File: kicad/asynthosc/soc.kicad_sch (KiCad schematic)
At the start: 1 part, among them U2 STM32H723ZGTx

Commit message: sch: wip
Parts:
- added C18, C19, C20, C21, C22, C23, C24, C25, C26, C27, C28: 100n, 0402, symbol Device:C
- added C29: 1u, 0402, symbol Device:C
- added FB2: BLM15PX330SN1D, 0402, symbol Device:FerriteBead
- added J13: RJ45_LED, symbol Connector:RJ45_LED
- added JP1: SolderJumper_2_Bridged, symbol Jumper:SolderJumper_2_Bridged
- added TR1: PT61017PEL, Transformer_SMD:Transformer_Ethernet_Bourns_PT61017PEL, symbol Transformer:PT61017PEL
- added U10: USBLC6-2P6, Package_TO_SOT_SMD:SOT-666, symbol Power_Protection:USBLC6-2P6
- added U9: LAN8742A, Package_DFN_QFN:VQFN-24-1EP_4x4mm_P0.5mm_EP2.5x2.5mm_ThermalVias, symbol Interface_Ethernet:LAN8742A
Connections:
- net 3V3: now also U2.108 (VDD), U2.121 (VDD), U2.131 (VDD), U2.144 (VDD), U2.17 (VDD), U2.30 (VDD), U2.39 (VDD), U2.52 (VDD), U2.62 (VDD), U2.72 (VDD), U2.84 (VDD), C18.1, C19.1, C20.1, C21.1, C22.1, C23.1, C24.1, C25.1, C26.1, C27.1, C28.1, FB2.1, JP1.2 (B)
- net GND: now also U2.107 (VSS), U2.120 (VSS), U2.130 (VSS), U2.16 (VSS), U2.31 (VSSA), U2.38 (VSS), U2.51 (VSS), U2.61 (VSS), U2.83 (VSS), U2.94 (VSS), C18.2, C19.2, C20.2, C21.2, C22.2, C23.2, C24.2, C25.2, C26.2, C27.2, C28.2, C29.2
- net at U2.33 (VDDA): now also FB2.2
- net at U2.6 (VBAT): now also C29.1, JP1.1 (A)
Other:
- moved on the sheet: U2

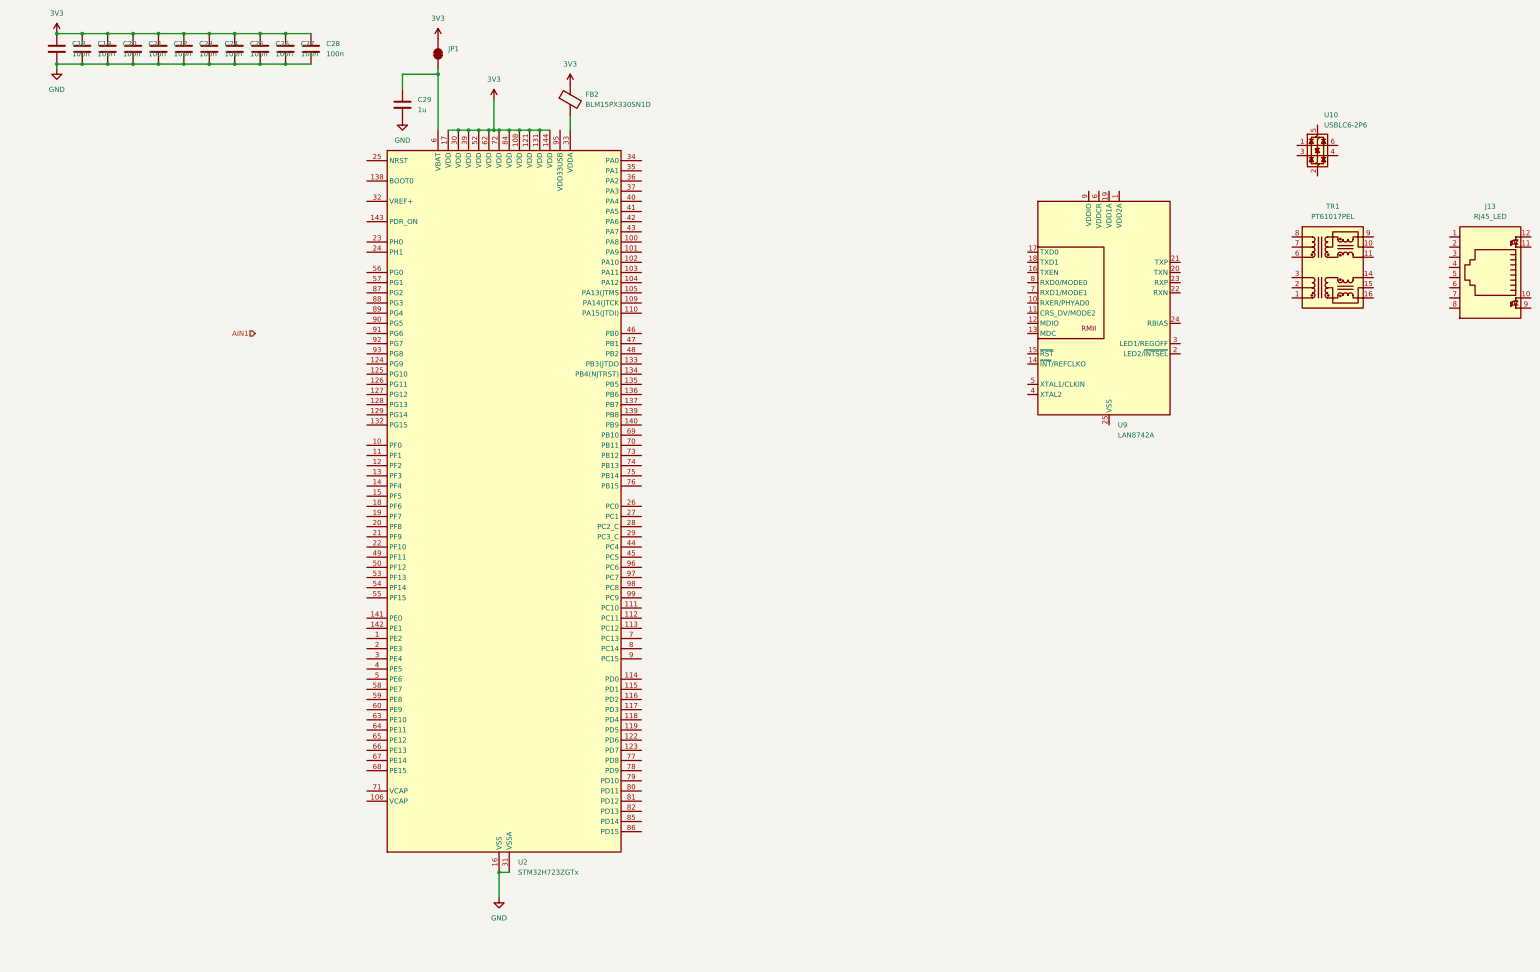
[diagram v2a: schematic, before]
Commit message: sch: basic stm32 with power, clocks and debug
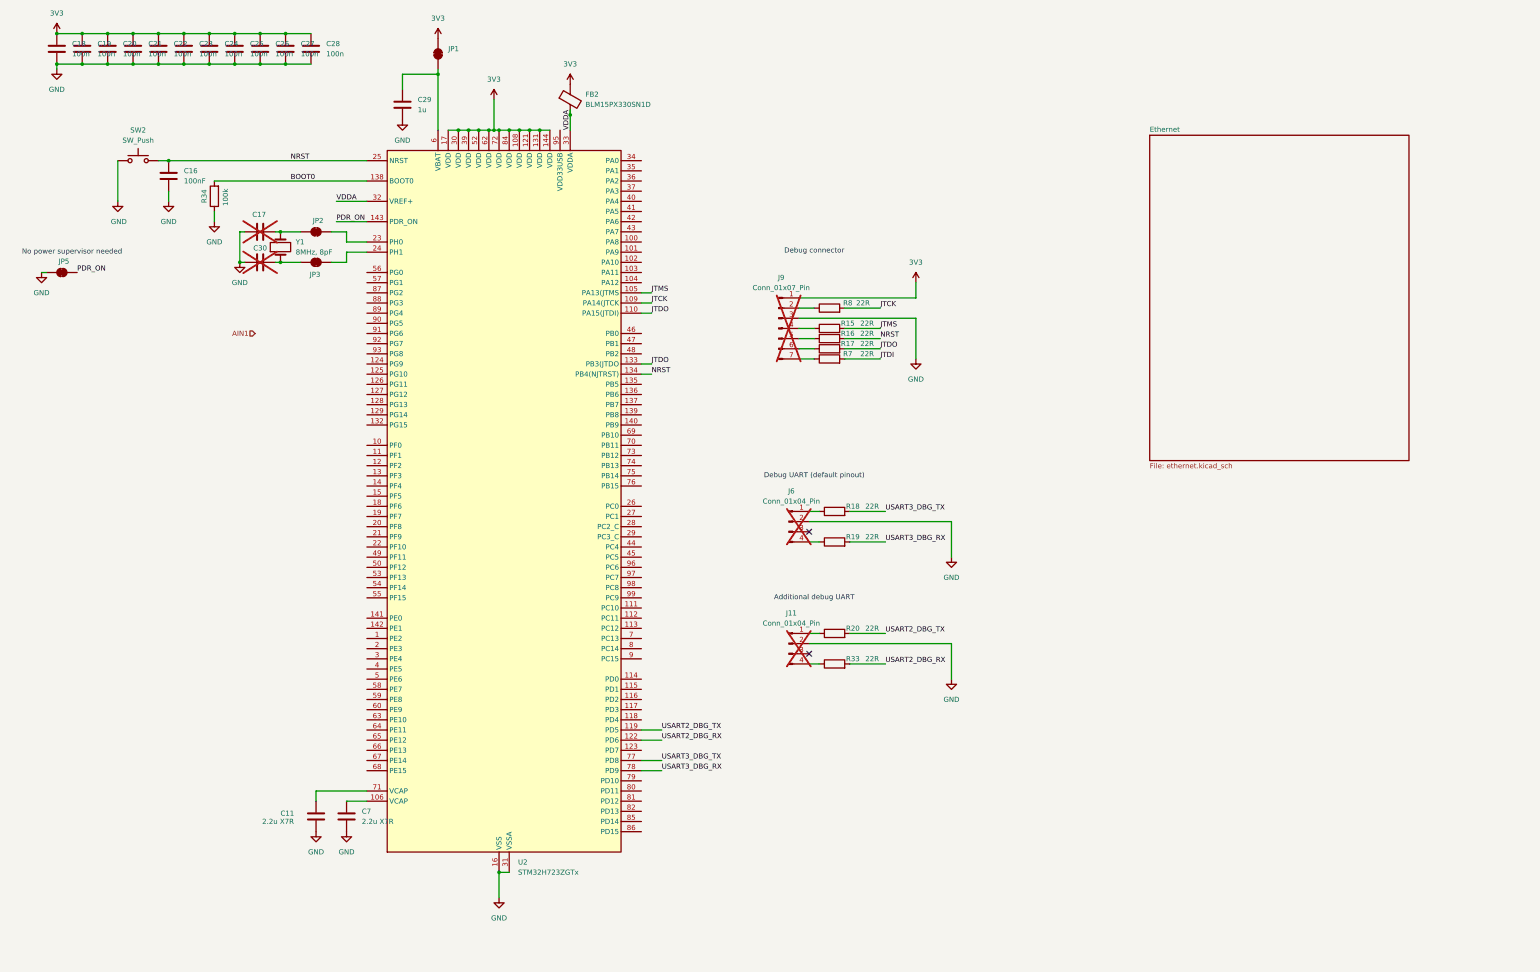
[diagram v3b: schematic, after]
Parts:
- removed J13: RJ45_LED, symbol Connector:RJ45_LED
- removed TR1: PT61017PEL, Transformer_SMD:Transformer_Ethernet_Bourns_PT61017PEL, symbol Transformer:PT61017PEL
- removed U10: USBLC6-2P6, Package_TO_SOT_SMD:SOT-666, symbol Power_Protection:USBLC6-2P6
- removed U9: LAN8742A, Package_DFN_QFN:VQFN-24-1EP_4x4mm_P0.5mm_EP2.5x2.5mm_ThermalVias, symbol Interface_Ethernet:LAN8742A
- added C11, C7: 2.2u X7R, 1206, symbol Device:C
- added C16: 100nF, 0402, symbol Device:C
- added C17, C30: 4.3pF, 0402, symbol Device:C
- added J11, J6: Conn_01x04_Pin, symbol Connector:Conn_01x04_Pin
- added J9: Conn_01x07_Pin, symbol Connector:Conn_01x07_Pin
- added JP2, JP3, JP5: SolderJumper_2_Bridged, symbol Jumper:SolderJumper_2_Bridged
- added R15, R16, R17, R18, R19, R20, R33, R7, R8: 22R, 0402, symbol Device:R
- added R34: 100k, 0402, symbol Device:R
- added SW2: SW_Push, symbol Switch:SW_Push
- added Y1: 8MHz, 8pF, symbol Device:Crystal
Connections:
- net 3V3: now also J9.1 (Pin_1)
- net GND: now also C11.2, C16.2, C17.1, C30.1, C7.2, J11.2 (Pin_2), J6.2 (Pin_2), J9.3 (Pin_3), JP5.2 (B), R34.1, SW2.1
- net JTMS: now reaches U2.105 (PA13(JTMS)
- net JTMS: now also R15.2
- net at U2.106 (VCAP): now also C7.1
- net JTCK: now reaches U2.109 (PA14(JTCK)
- net JTCK: now also R8.2
- net JTDO: now reaches U2.110 (PA15(JTDI))
- net JTDO: now also U2.133 (PB3(JTDO), R17.2
- net USART2_DBG_TX: now reaches U2.119 (PD5)
- net USART2_DBG_TX: now also R20.2
- net USART2_DBG_RX: now reaches U2.122 (PD6)
- net USART2_DBG_RX: now also R33.2
- net NRST: now reaches U2.134 (PB4(NJTRST))
- net NRST: now also U2.25 (NRST), C16.1, R16.2, SW2.2
- net BOOT0: now reaches U2.138 (BOOT0)
- net BOOT0: now also R34.2
- net PDR_ON: now reaches U2.143 (PDR_ON)
- net PDR_ON: now also JP5.1 (A)
- net at U2.23 (PH0): now also JP2.1 (A)
- net at U2.24 (PH1): now also JP3.1 (A)
- net VDDA: now reaches U2.32 (VREF+)
- net VDDA: now also FB2.2, U2.33 (VDDA)
- net at U2.71 (VCAP): now also C11.1
- net USART3_DBG_TX: now reaches U2.77 (PD8)
- net USART3_DBG_TX: now also R18.2
- net USART3_DBG_RX: now reaches U2.78 (PD9)
- net USART3_DBG_RX: now also R19.2
- new net: C30.2, JP3.2 (B), Y1.1
- new net: C17.2, JP2.2 (B), Y1.2
- new net: J11.1 (Pin_1), R20.1
- new net: J11.4 (Pin_4), R33.1
- new net: J9.4 (Pin_4), R15.1
- new net: J6.1 (Pin_1), R18.1
- new net: J9.7 (Pin_7), R7.1
- new net: J9.6 (Pin_6), R17.1
- new net: J9.2 (Pin_2), R8.1
- new net: J6.4 (Pin_4), R19.1
- new net: J9.5 (Pin_5), R16.1
- new net JTDI: R7.2
- no-connect marks 0 -> 2
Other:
- added sheet Ethernet (ethernet.kicad_sch)
- note added: "Additional debug UART"
- note added: "Debug UART (default pinout)"
- note added: "Debug connector"
- note added: "No power supervisor needed"

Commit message: sch: rmii side
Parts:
- added R61: 10k, 0402, symbol Device:R
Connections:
- net 3V3: now also U2.95 (VDD33USB)
- net at U2.101 (PA9): now also R61.2
- net USB_ID: now reaches U2.102 (PA10)
- net USB_D_N: now reaches U2.103 (PA11)
- net USB_D_P: now reaches U2.104 (PA12)
- new net USB_VBUS: R61.1
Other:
- sheet Ethernet ports: added RMII_CRS_DV, RMII_MDC, RMII_MDIO, RMII_NRST, RMII_REF_CLK, RMII_RXD0, RMII_RXD1, RMII_TXD0, RMII_TXD1, RMII_TX_EN; removed none
- moved on the sheet: FB2, J11, J6, J9, R15, R16, R17, R18, R19, R20, R33, R7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

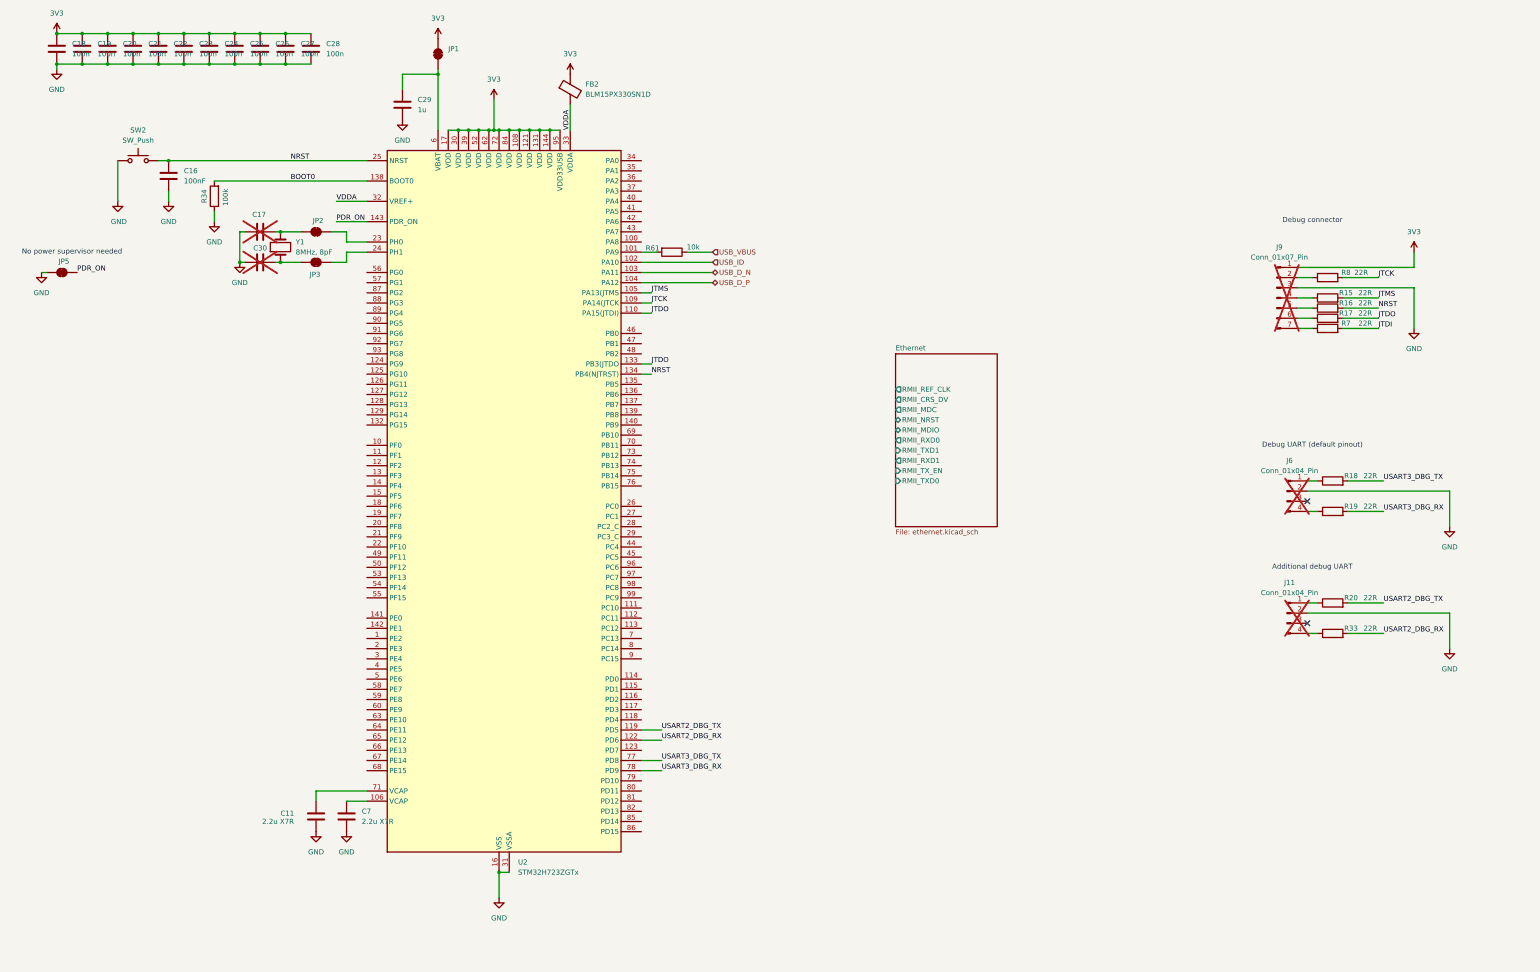
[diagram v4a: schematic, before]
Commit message: sch: top sheet pins input
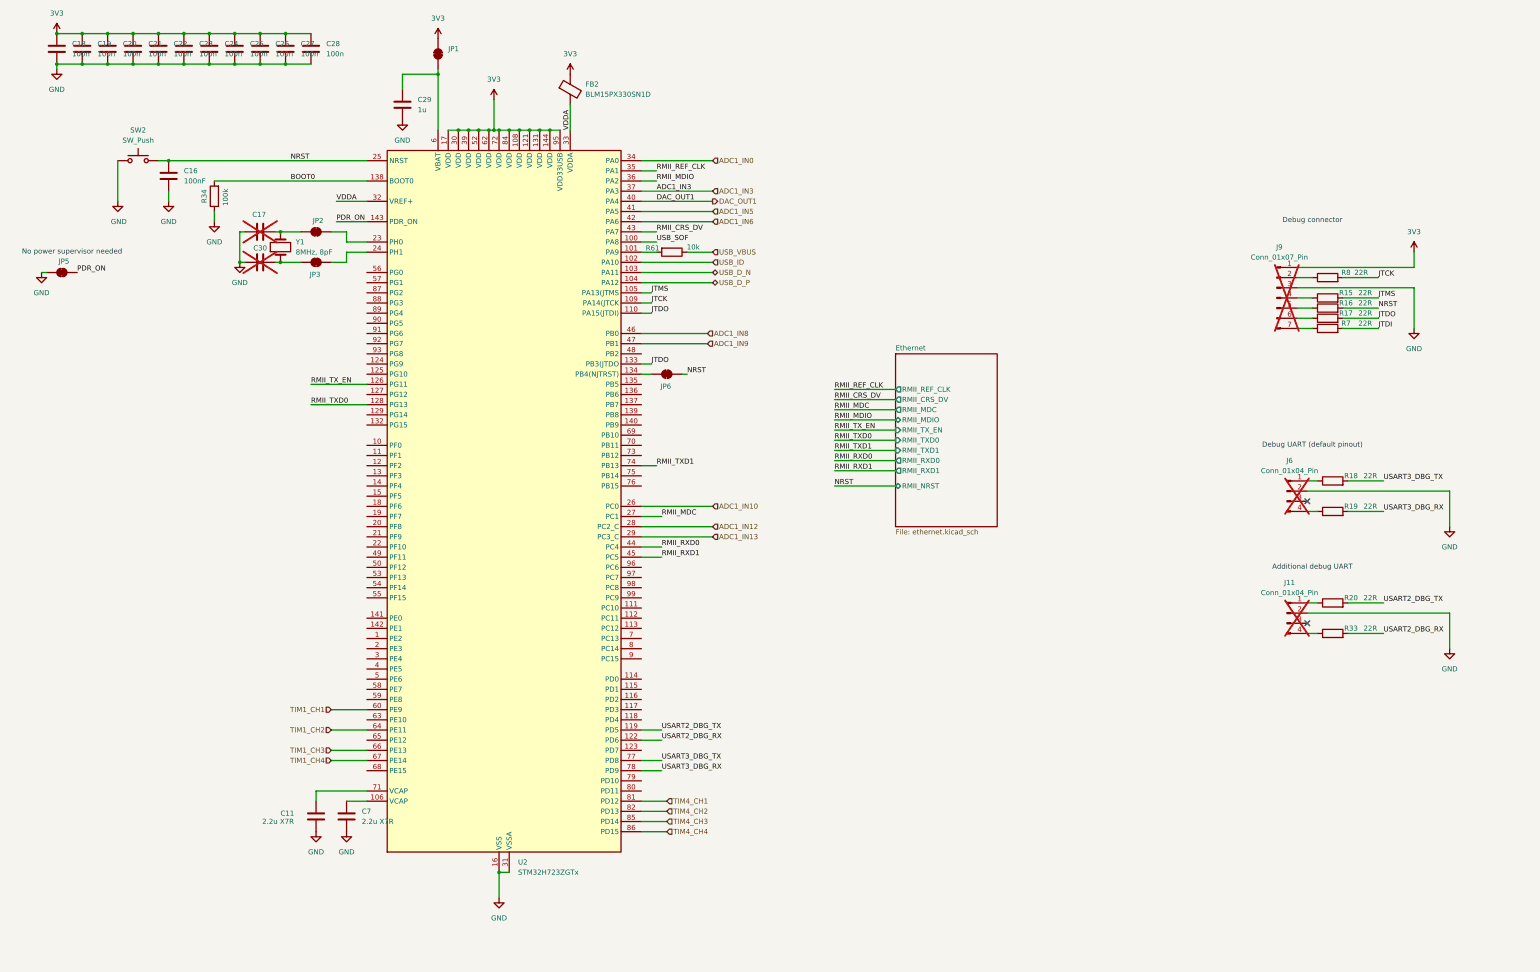
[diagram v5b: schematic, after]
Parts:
- added JP6: SolderJumper_2_Bridged, symbol Jumper:SolderJumper_2_Bridged
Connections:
- net NRST: now also JP6.1 (A); no longer U2.134 (PB4(NJTRST))
- net USB_SOF: now reaches U2.100 (PA8)
- net RMII_TX_EN: now reaches U2.126 (PG11)
- net RMII_TXD0: now reaches U2.128 (PG13)
- net ADC1_IN10: now reaches U2.26 (PC0)
- net RMII_MDC: now reaches U2.27 (PC1)
- net ADC1_IN12: now reaches U2.28 (PC2_C)
- net ADC1_IN13: now reaches U2.29 (PC3_C)
- net ADC1_IN0: now reaches U2.34 (PA0)
- net RMII_REF_CLK: now reaches U2.35 (PA1)
- net RMII_MDIO: now reaches U2.36 (PA2)
- net ADC1_IN3: now reaches U2.37 (PA3)
- net DAC_OUT1: now reaches U2.40 (PA4)
- net ADC1_IN5: now reaches U2.41 (PA5)
- net ADC1_IN6: now reaches U2.42 (PA6)
- net RMII_CRS_DV: now reaches U2.43 (PA7)
- net RMII_RXD0: now reaches U2.44 (PC4)
- net RMII_RXD1: now reaches U2.45 (PC5)
- net ADC1_IN8: now reaches U2.46 (PB0)
- net ADC1_IN9: now reaches U2.47 (PB1)
- net TIM1_CH1: now reaches U2.60 (PE9)
- net TIM1_CH2: now reaches U2.64 (PE11)
- net TIM1_CH3: now reaches U2.66 (PE13)
- net TIM1_CH4: now reaches U2.67 (PE14)
- net RMII_TXD1: now reaches U2.74 (PB13)
- net TIM4_CH1: now reaches U2.81 (PD12)
- net TIM4_CH2: now reaches U2.82 (PD13)
- net TIM4_CH3: now reaches U2.85 (PD14)
- net TIM4_CH4: now reaches U2.86 (PD15)
- new net: JP6.2 (B), U2.134 (PB4(NJTRST))

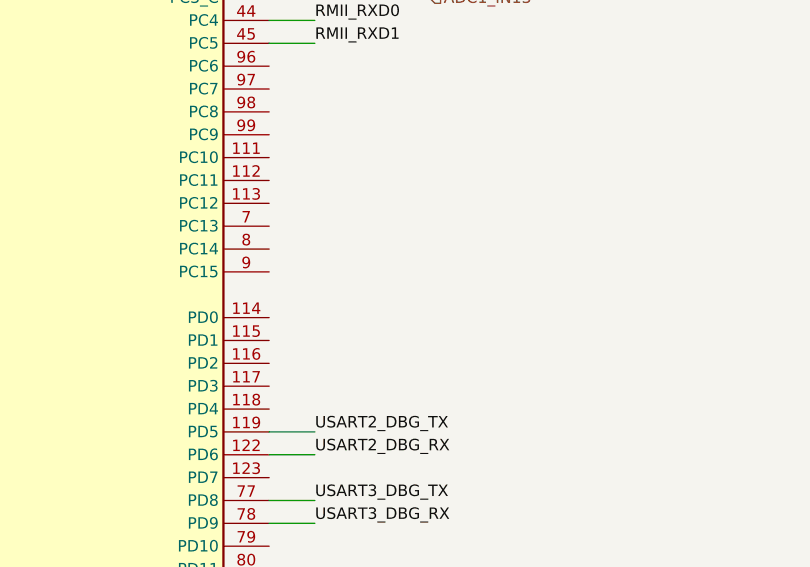
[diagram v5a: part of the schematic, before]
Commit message: sch: update and new interface sheet
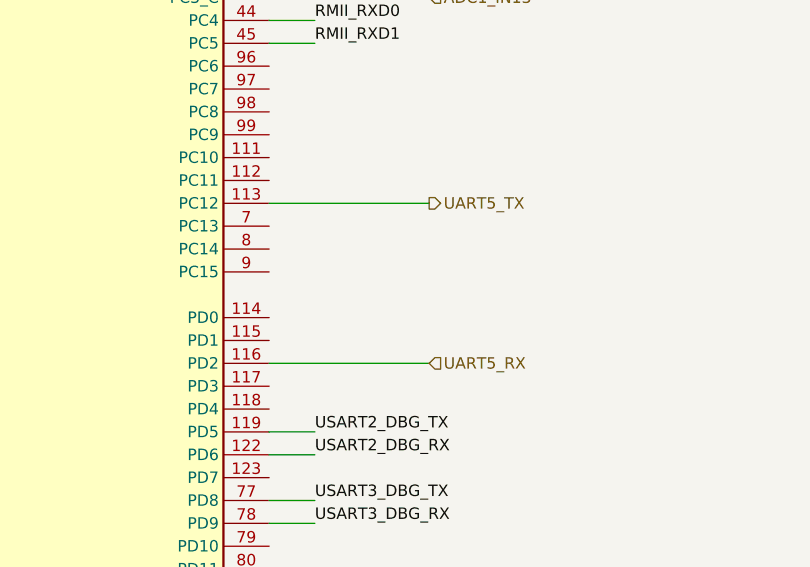
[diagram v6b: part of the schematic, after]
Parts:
- C11, C7: footprint 1206 -> (none)
- C16, C17, C18, C19, C20, C21, C22, C23, C24, C25, C26, C27, C28, C29, C30, FB2, R15, R16, R17, R18, R19, R20, R33, R34, R61, R7, R8: footprint 0402 -> (none)
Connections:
- net UART5_TX: now reaches U2.113 (PC12)
- net UART5_RX: now reaches U2.116 (PD2)
